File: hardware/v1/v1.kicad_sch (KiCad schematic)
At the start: 27 parts

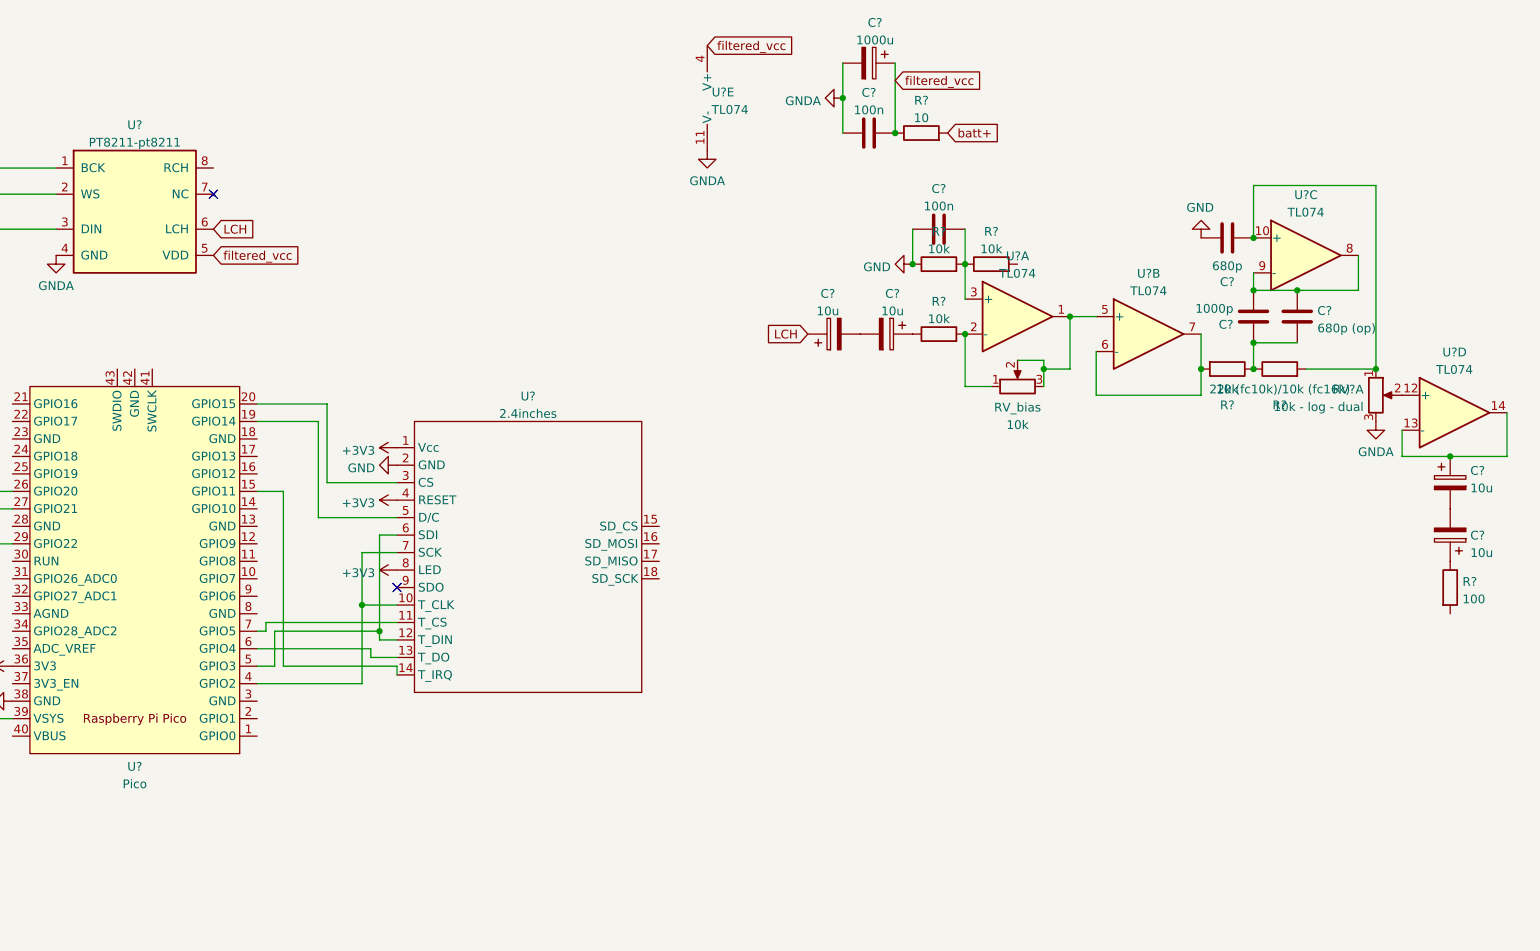
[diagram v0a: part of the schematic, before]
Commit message: Second output filter
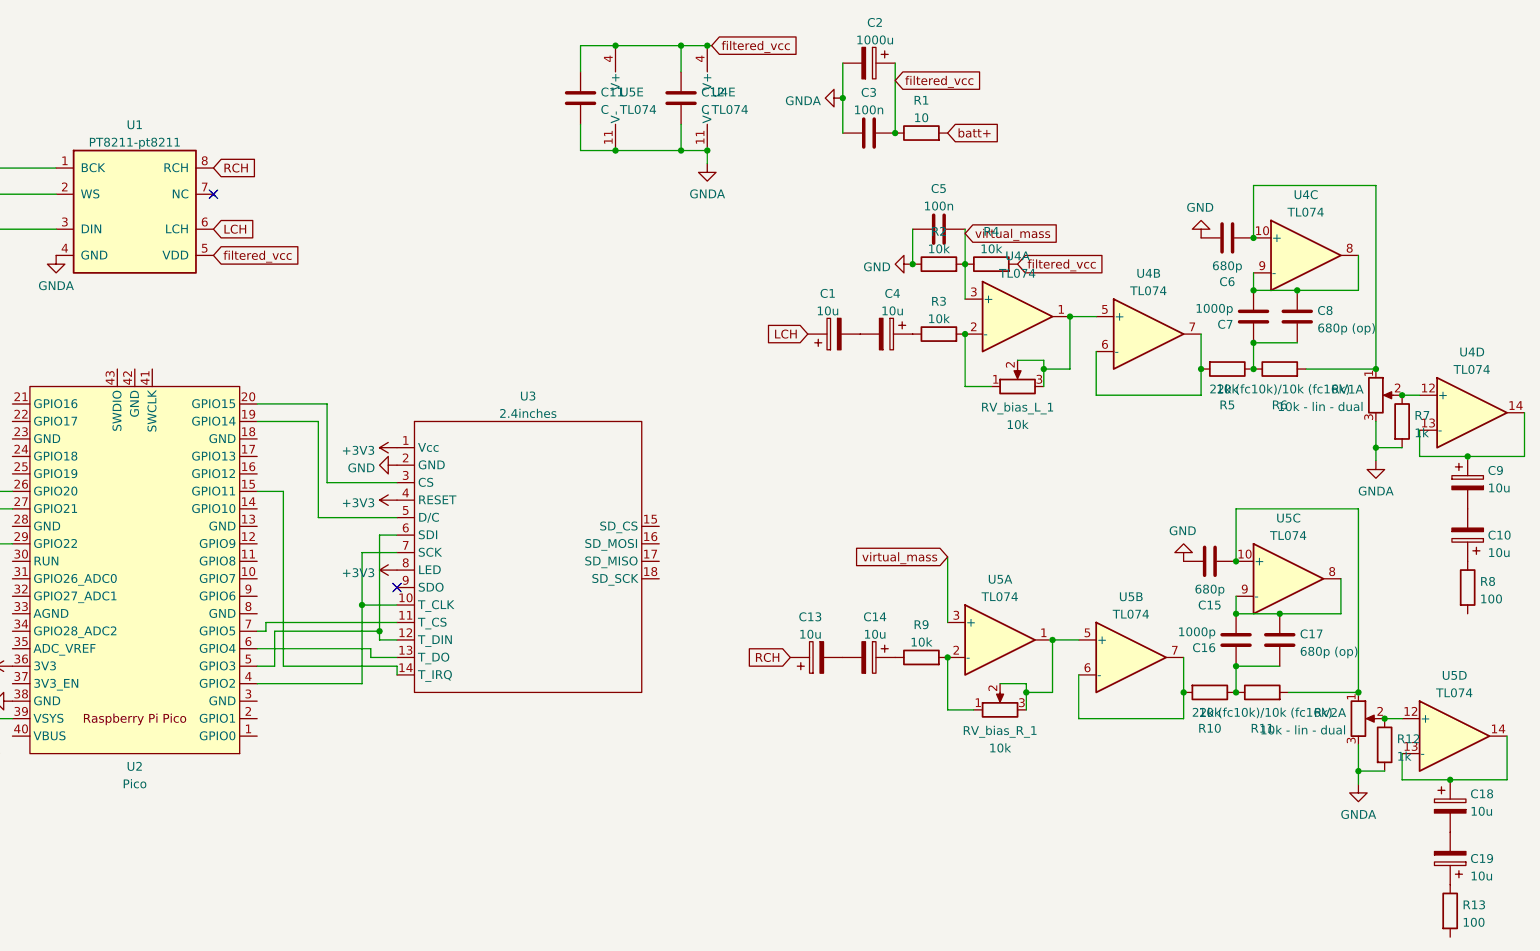
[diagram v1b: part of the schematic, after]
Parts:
- added C11, C12: C, symbol Device:C
- added C13, C14: 10u, Capacitor_THT:CP_Radial_D5.0mm_P2.50mm, symbol Device:C_Polarized
- added C15: 680p, Capacitor_THT:C_Disc_D5.0mm_W2.5mm_P2.50mm, symbol Device:C
- added C16: 1000p, Capacitor_THT:C_Disc_D5.0mm_W2.5mm_P2.50mm, symbol Device:C
- added C17: 680p (op), Capacitor_THT:C_Disc_D3.8mm_W2.6mm_P2.50mm, symbol Device:C
- added C18, C19: 10u, symbol Device:C_Polarized
- added R10, R9: 10k, Resistor_THT:R_Axial_DIN0207_L6.3mm_D2.5mm_P7.62mm_Horizontal, symbol Device:R
- added R11: 22k (fc10k)/10k (fc16k), Resistor_THT:R_Axial_DIN0207_L6.3mm_D2.5mm_P7.62mm_Horizontal, symbol Device:R
- added R12, R7: 1k, symbol Device:R
- added R13: 100, symbol Device:R
- added RV2: 10k - lin - dual, symbol Device:R_Potentiometer_Dual_Separate
- added RV_bias_R_1: 10k, Potentiometer_THT:Potentiometer_Runtron_RM-065_Vertical, symbol Device:R_Potentiometer
- added U5: TL074, Package_DIP:DIP-14_W7.62mm_Socket, symbol Amplifier_Operational:TL074
- RV1: renamed from RV?; value 10k - log - dual -> 10k - lin - dual
- gave numbers to parts that had none: 21
- renumbered RV_bias to RV_bias_L_1
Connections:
- net GND: now also C15.1
- net GNDA: now also C11.2, C12.2, R12.2, R7.2, RV2.3, U5.11 (V-)
- net filtered_vcc: now also R4.2, C11.1, C12.1, U5.4 (V+)
- net virtual_mass: now reaches C5.2, R2.2, R4.1, U4.3 (+)
- net virtual_mass: now also U5.3 (+)
- net at RV1.2, U4.12 (+): now also R7.1
- net RCH: now reaches U1.8 (RCH)
- net RCH: now also C13.1
- new net: C15.2, R11.2, RV2.1, U5.10 (+)
- new net: C16.2, C17.1, U5.8, U5.9 (-)
- new net: C16.1, C17.2, R10.1, R11.1
- new net: R10.2, U5.6 (-), U5.7
- new net: C19.1, R13.1
- new net: RV_bias_R_1.2, RV_bias_R_1.3, U5.1, U5.5 (+)
- new net: R12.1, RV2.2, U5.12 (+)
- new net: C18.2, C19.2
- new net: C14.1, R9.1
- new net: C13.2, C14.2
- new net: R9.2, RV_bias_R_1.1, U5.2 (-)
- new net: C18.1, U5.13 (-), U5.14
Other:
- moved on the sheet: C10, C9, R8, U4D

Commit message: Added input audio to schema
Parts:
- added AudioIn_gain_R_?: 10k, Potentiometer_THT:Potentiometer_Runtron_RM-065_Vertical, symbol Device:R_Potentiometer
- added C? (x2): 10u, symbol Device:C_Polarized
- added J?: AudioJack3_Switch, symbol Connector:AudioJack3_Switch
- added R?: 10k, symbol Device:R
- added RV?: R_Potentiometer, symbol Device:R_Potentiometer
- added U? (x2): TL072, symbol Amplifier_Operational:TL072
- renumbered RV_bias_L_1 to RV_gain_L_1, RV_bias_R_1 to RV_gain_R_1
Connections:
- net GND: now also J?.S; no longer C15.1, C5.1, C6.1, R2.1
- net GNDA: now also C15.1, C5.1, C6.1, R2.1, RV?.3
- net virtual_mass: now also U?.3 (+)
- net at U2.31 (GPIO26_ADC0): now also RV?.2, U?.6 (-), U?.7
- net ADC_VREF: now reaches U2.35 (ADC_VREF)
- net ADC_VREF: now also RV?.1
- net +3.3VA renamed batt+
- new net: AudioIn_gain_R_?.2, AudioIn_gain_R_?.3, U?.1, U?.5 (+)
- new net: AudioIn_gain_R_?.1, R?.2, U?.2 (-)
- new net: C?.1, J?.T
- new net: C?.2, C?.2
- new net: C?.1, R?.1
- no-connect marks 2 -> 6
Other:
- note added: "OR"

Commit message: Finished audio output schema, add midi in
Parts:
- removed C1, C13, C14: 10u, Capacitor_THT:CP_Radial_D5.0mm_P2.50mm, symbol Device:C_Polarized
- removed C10, C9: 10u, symbol Device:C_Polarized
- removed C17: 680p (op), Capacitor_THT:C_Disc_D3.8mm_W2.6mm_P2.50mm, symbol Device:C
- removed C5: 100n, Capacitor_THT:C_Disc_D4.7mm_W2.5mm_P5.00mm, symbol Device:C
- removed C6: 680p, Capacitor_THT:C_Disc_D5.0mm_W2.5mm_P2.50mm, symbol Device:C
- removed C7: 1000p, Capacitor_THT:C_Disc_D5.0mm_W2.5mm_P2.50mm, symbol Device:C
- added C1: C, symbol Device:C
- added C10, C9: 680p, Capacitor_THT:C_Disc_D5.0mm_W2.5mm_P2.50mm, symbol Device:C
- added C13, C14: 1000p, Capacitor_THT:C_Disc_D5.0mm_W2.5mm_P2.50mm, symbol Device:C
- added C17, C22: 10u, symbol Device:C_Polarized
- added C5, C6, C7: 10u, Capacitor_THT:CP_Radial_D5.0mm_P2.50mm, symbol Device:C_Polarized
- added C?: 100n, symbol Device:C
- added C?: 100u, symbol Device:C_Polarized
- added D?: 1N914, symbol Device:D
- added J?: MIDI IN, symbol Connector:DIN-5
- added J? (x2): AudioJack3_Switch, symbol Connector:AudioJack3_Switch
- added R? (x2): 220, symbol Device:R
- added RV?: 10k - POT2, symbol Device:R_Potentiometer
- added RV?: 10k - POT1, symbol Device:R_Potentiometer
- added unit 3 of U6
- added U?: 6N138, symbol Isolator:6N138
- C15: value 680p -> 680p (op); footprint Capacitor_THT:C_Disc_D5.0mm_W2.5mm_P2.50mm -> Capacitor_THT:C_Disc_D3.8mm_W2.6mm_P2.50mm
- C16: value 1000p -> 680p (op); footprint Capacitor_THT:C_Disc_D5.0mm_W2.5mm_P2.50mm -> Capacitor_THT:C_Disc_D3.8mm_W2.6mm_P2.50mm
- C8: value 680p (op) -> 100n; footprint Capacitor_THT:C_Disc_D3.8mm_W2.6mm_P2.50mm -> Capacitor_THT:C_Disc_D4.7mm_W2.5mm_P5.00mm
- R10: value 10k -> 1k; footprint Resistor_THT:R_Axial_DIN0207_L6.3mm_D2.5mm_P7.62mm_Horizontal -> (none)
- R11: value 22k (fc10k)/10k (fc16k) -> 1k; footprint Resistor_THT:R_Axial_DIN0207_L6.3mm_D2.5mm_P7.62mm_Horizontal -> (none)
- R12: value 1k -> 100
- R6: value 22k (fc10k)/10k (fc16k) -> 10k
- R7: value 1k -> 10k; footprint (none) -> Resistor_THT:R_Axial_DIN0207_L6.3mm_D2.5mm_P7.62mm_Horizontal
- R8: value 100 -> 22k (fc10k)/10k (fc16k); footprint (none) -> Resistor_THT:R_Axial_DIN0207_L6.3mm_D2.5mm_P7.62mm_Horizontal
- R9: value 10k -> 22k (fc10k)/10k (fc16k)
- RV3: renamed from RV?; value R_Potentiometer -> 10k - POT0
- gave numbers to parts that had none: 6
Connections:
- net ADC_VREF: now also RV?.1, RV?.1
- net GND: now also C?.1, C?.2, U?.5 (GND)
- net GNDA: now also C8.1, R10.2, R11.2, R3.1, C1.2, C10.1, C9.1, J?.S, J?.S, RV?.3, RV?.3, U6.4 (V-); no longer C15.1, R12.2, R2.1, R7.2
- net LCH: now also C5.1
- net RCH: now also C4.1
- net filtered_vcc: now also R5.2, C1.1, U6.8 (V+); no longer R4.2
- net virtual_mass: now also C8.2, R3.2, R5.1; no longer R2.2, R4.1
- net at RV2.1, U5.10 (+): now also R9.2, C10.2; no longer C15.2, R11.2
- net at RV1.2, U4.12 (+): now also R10.1; no longer R7.1
- net at U4.13 (-), U4.14: now also C17.1
- net at U4.8, U4.9 (-): now also C15.1, C13.2; no longer C8.1
- net at U5.8, U5.9 (-): now also C16.1, C14.2; no longer C16.2
- net at R8.1: now also C15.2, R6.1, C13.1
- net at U5.6 (-), U5.7: now also R7.2; no longer R10.2
- net at R8.2: now also RV1.1, U4.10 (+), C9.2
- net at C19.1: now also U5.13 (-), U5.14; no longer R13.1
- net at R13.2: now also J?.T
- net at U5.1, U5.5 (+): now also RV_gain_L_1.2, RV_gain_L_1.3; no longer RV_gain_R_1.2, RV_gain_R_1.3
- net at U4.1, U4.5 (+): now also RV_gain_R_1.2, RV_gain_R_1.3; no longer RV_gain_L_1.2, RV_gain_L_1.3
- net at RV2.2, U5.12 (+): now also R11.1; no longer R12.1
- net at U4.6 (-), U4.7: now also R6.2; no longer R5.2
- net at C4.2: now also C6.2
- net at C19.2: now also C22.2; no longer C18.2
- net at R9.1: now also C16.2, R7.1, C14.1
- net at U2.2 (GPIO1): now also R?.1, U?.6 (VO2)
- net at U2.32 (GPIO27_ADC1): now also RV?.2
- net at U2.34 (GPIO28_ADC2): now also RV?.2
- new net: C7.1, R4.1
- new net: C5.2, C7.2
- new net: J?.4, R?.2
- new net: D?.2 (A), J?.5, U?.3 (C2)
- new net: C22.1, R13.1
- new net: R4.2, RV_gain_L_1.1, U5.2 (-)
- new net: D?.1 (K), R?.1, U?.2 (C1)
- new net: R2.2, RV_gain_R_1.1, U4.2 (-)
- new net: C17.2, C18.2
- new net: C18.1, R12.1
- new net: J?.T, R12.2
- new net: C6.1, R2.1
- new net +3.3V: C?.1, C?.2, R?.2, U?.8 (VCC)
- new net batt-: J?.R
- no-connect marks 6 -> 17
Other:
- added sheet audio_output (audio_output.kicad_sch)
- note added: "Powering on jack insert"

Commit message: Added expression pedals
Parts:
- removed J?: MIDI IN, symbol Connector:DIN-5
- added J2: DIN-5_180degree, symbol Connector:DIN-5_180degree
- added J3: MIDI IN, symbol Connector:DIN-5_180degree
- added J4: MIDI THRU, symbol Connector:DIN-5_180degree
- added J7: EXP 2, symbol Connector:AudioJack3_Switch
- added J8: EXP 1, symbol Connector:AudioJack3_Switch
- added R15, R19: 33, symbol Device:R
- added R16, R20: 10, symbol Device:R
- J5: renamed from J?; value AudioJack3_Switch -> OUTPUT R
- J6: renamed from J?; value AudioJack3_Switch -> OUTPUT L - MONO
- gave numbers to parts that had none: 8
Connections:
- net +3.3V: now also R15.2, R19.2
- net ADC_VREF: now also J7.T, J8.T
- net GND: now also J2.2, J4.2
- net GNDA: now also U2.33 (AGND), J7.S, J8.S
- net at R18.2: now also J3.4
- net at D1.2 (A), U7.3 (C2): now also J3.5
- net at RV4.2, U2.34 (GPIO28_ADC2): now also J7.R
- net at RV5.2, U2.32 (GPIO27_ADC1): now also J8.R
- net at R17.1, U2.2 (GPIO1), U7.6 (VO2): now also R20.1
- net at U2.1 (GPIO0): now also R16.1
- new net: J4.4, R19.1
- new net: J4.5, R20.2
- new net: J2.4, R15.1
- new net: J2.5, R16.2
- no-connect marks 17 -> 27
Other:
- moved on the sheet: C23, C24, D1, R17, R18, U3, U7

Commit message: Added rotary, and SD SPI card. Tested rotary
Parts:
- added SW?: RotaryEncoder_Switch, symbol Device:RotaryEncoder_Switch
- J2: value DIN-5_180degree -> MIDI OUT
- renumbered AudioIn_gain_R_1 to AudioIn_gain_trim_R_1, RV_gain_L_1 to RV_gain_trim_L_1, RV_gain_R_1 to RV_gain_trim_R_1
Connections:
- net GND: now also SW?.C, SW?.S2
- net at U2.10 (GPIO7): now also SW?.A
- net at U2.15 (GPIO11): no longer U3.14 (T_IRQ)
- net at U2.21 (GPIO16): now also SW?.S1
- net at U2.24 (GPIO18): now also U3.14 (T_IRQ)
- net at U2.25 (GPIO19): now also U3.15 (SD_CS)
- net at U2.4 (GPIO2), U3.10 (T_CLK), U3.7 (SCK): now also U3.18 (SD_SCK)
- net at U2.5 (GPIO3), U3.12 (T_DIN), U3.6 (SDI): now also U3.16 (SD_MOSI)
- net at U2.6 (GPIO4), U3.13 (T_DO): now also U3.17 (SD_MISO)
- net at U2.9 (GPIO6): now also SW?.B
- no-connect marks 27 -> 45

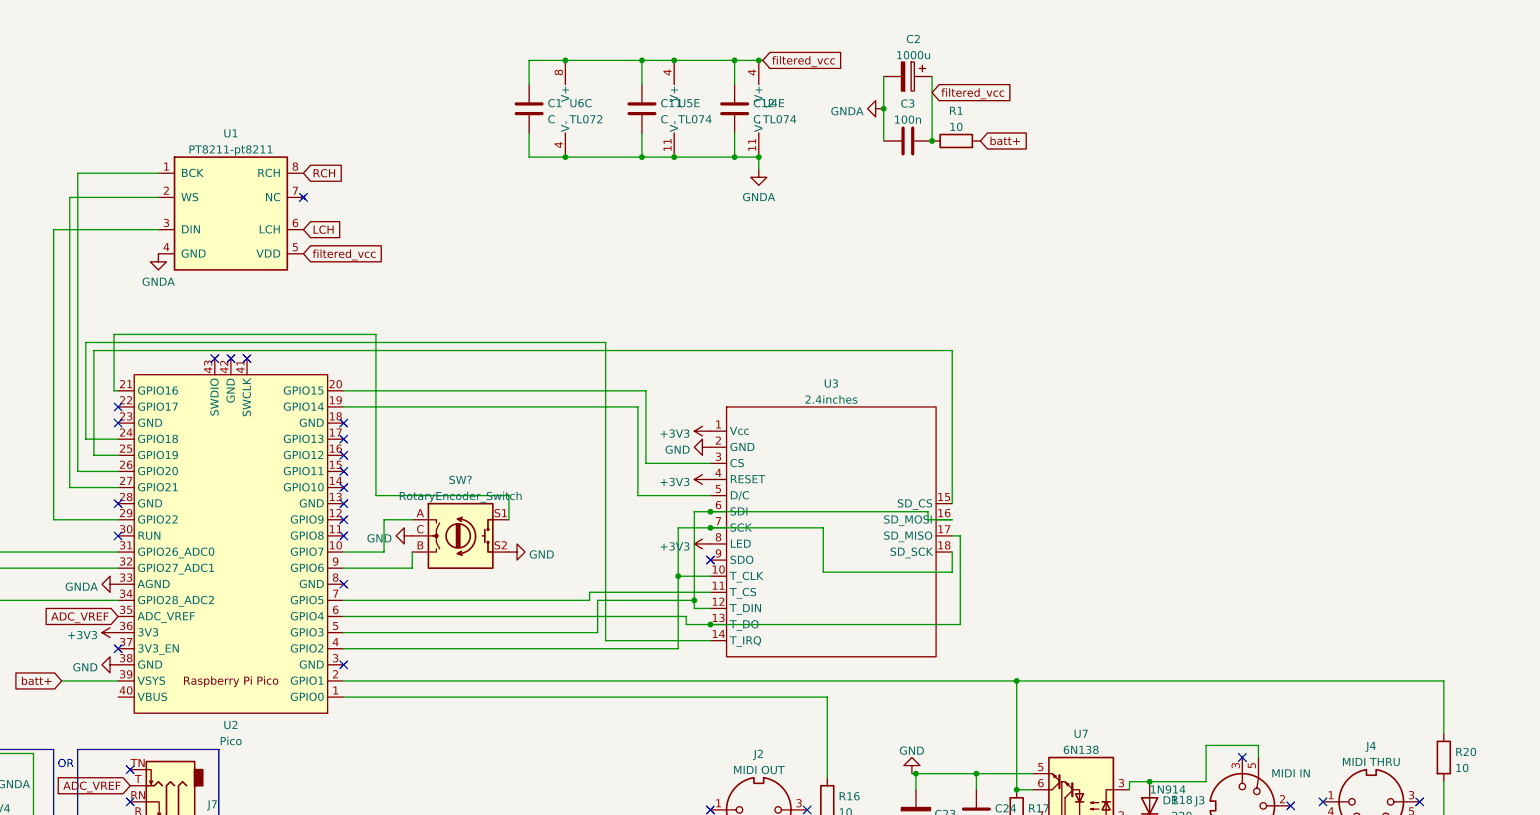
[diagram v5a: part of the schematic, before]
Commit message: Added battery connector, started symbol association
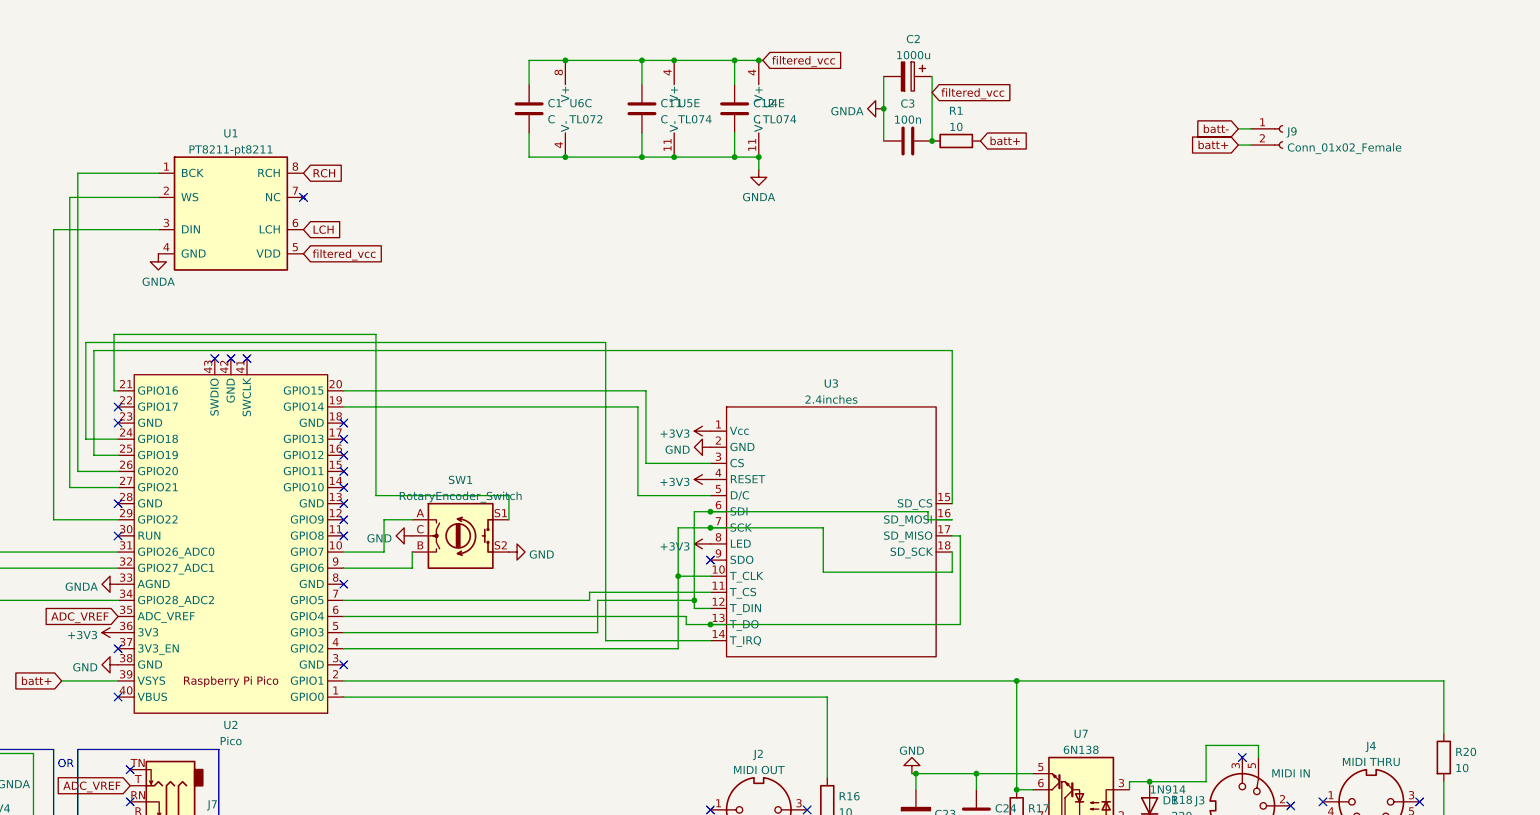
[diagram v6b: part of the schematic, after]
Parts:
- added J9: Conn_01x02_Female, symbol Connector:Conn_01x02_Female
- R10, R11, R12, R13, R14, R15, R16, R17, R18, R19, R20: footprint (none) -> Resistor_THT:R_Axial_DIN0207_L6.3mm_D2.5mm_P7.62mm_Horizontal
- U4, U5: footprint (none) -> Package_DIP:DIP-14_W7.62mm_Socket
- U6, U7: footprint (none) -> Package_DIP:DIP-8_W7.62mm_Socket
- gave numbers to parts that had none: 1
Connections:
- net batt+: now also J9.2 (Pin_2)
- net batt-: now also J9.1 (Pin_1)
- no-connect marks 45 -> 46

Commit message: Continued components assig
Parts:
- C1, C11, C12: value C -> 100n
- J1: value AudioJack3_Switch -> AUDIO IN; footprint (none) -> Connector_Audio:Jack_6.35mm_Neutrik_NMJ6HFD2_Horizontal
- J5, J6, J7, J8: footprint (none) -> Connector_Audio:Jack_6.35mm_Neutrik_NMJ6HFD2_Horizontal
- R1: footprint (none) -> Resistor_THT:R_Axial_DIN0207_L6.3mm_D2.5mm_P7.62mm_Horizontal
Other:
- moved on the sheet: C8, R3, R5
